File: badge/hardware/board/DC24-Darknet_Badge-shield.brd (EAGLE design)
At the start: 48.3 x 68.4 mm, 38 parts, among them SW0 SWITCH_TACTILETACTILE-2PIN-NA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, SW1 SWITCH_TACTILETACTILE-2PIN-NA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, SW2 SWITCH_TACTILETACTILE-2PIN-NA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, SW3 SWITCH_TACTILETACTILE-2PIN-NA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, SW4 SWITCH_TACTILETACTILE-2PIN-NA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, SW5 SWITCH_TACTILETACTILE-2PIN-NA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, SW6 SWITCH_TACTILETACTILE-2PIN-NA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, SW7 SWITCH_TACTILETACTILE-2PIN-NA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, SW8 SWITCH_TACTILETACTILE-2PIN-NA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, SW9 SWITCH_TACTILETACTILE-2PIN-NA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

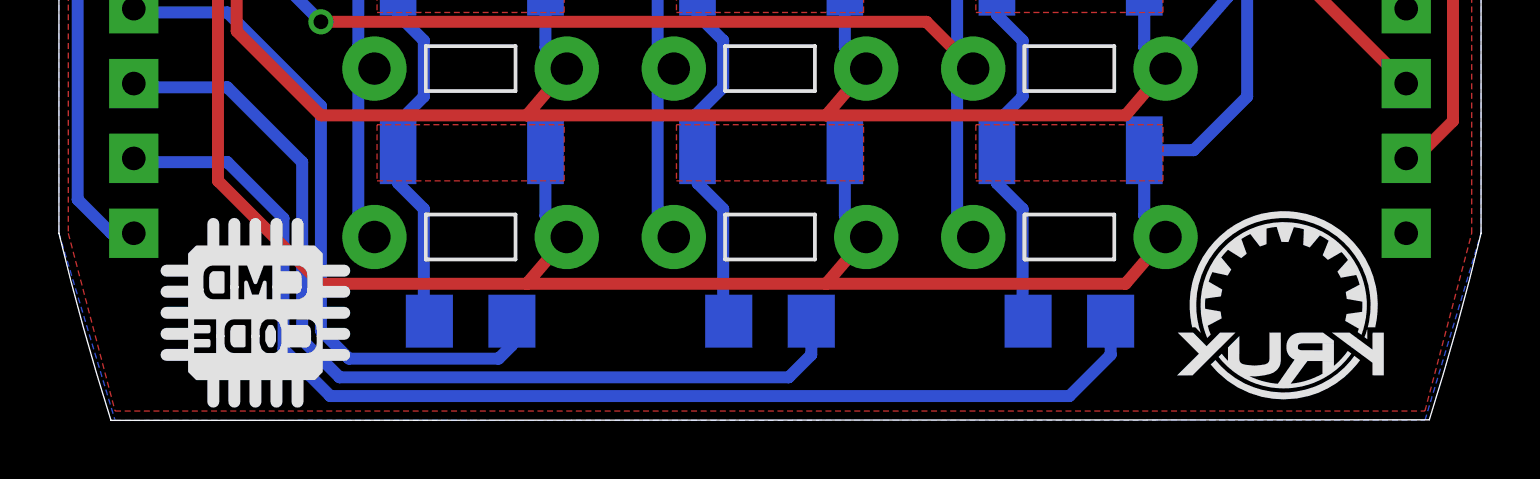
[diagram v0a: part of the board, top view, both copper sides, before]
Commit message: Board design that was made for DEF CON Note there are some problems with ground plane isolation that were not caught which makes this easy to accidentally bridge VCC and GND when soldering.
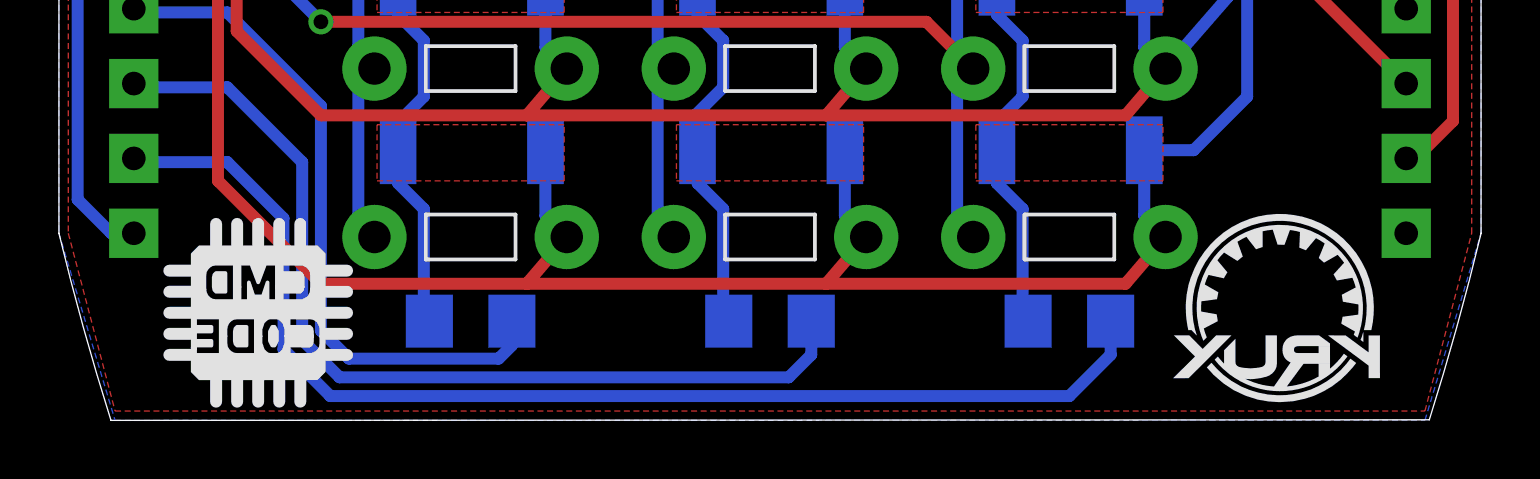
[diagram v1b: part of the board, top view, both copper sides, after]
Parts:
- moved U$21 0.16 mm to (97.3, 17.8)
- moved U$23 0.09 mm to (62.6, 17.9)
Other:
- board text added: "47"
